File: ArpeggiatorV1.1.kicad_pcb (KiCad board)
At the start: 2 copper layers, 100 x 100 mm, 67 parts, among them J1 DIN-5 MIDI_IN, J2 DIN-5 SYNC_IN, J3 DIN-5 MIDI_OUT, J4 Conn_01x03_Pin, SW1 SW_SYNC, SW2 SW_MODE, SW3 SW_OCT, SW4 SW_ONOFF, SW5 SW_HOLD, U1 6N138, U2 6N138, U3 Pico

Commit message: Minor PCB corrections and cleanups.
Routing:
- net GND: track 32.5 -> 0.00 mm
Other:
- board text added: "MIDI Sync"
- board text removed: "Tempo"
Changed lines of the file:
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@@
     (effects (font (size 2 2) (thickness 0.15)) (justify bottom mirror))
   )
-  (gr_text "Tempo" (at 43.18 123.952) (layer "F.SilkS")
+  (gr_text "MIDI Sync" (at 43.18 123.952) (layer "F.SilkS")
     (effects (font (size 1 1) (thickness 0.15)) (justify bottom))
   )
@@
   (segment (start 55.225 53.975) (end 57.785 56.535) (width 0.4) (layer "F.Cu") (net 1))
   (segment (start 46.99 50.165) (end 50.8 53.975) (width 0.4) (layer "F.Cu") (net 1))
-  (segment (start 132.79 130.52) (end 126.29 130.52) (width 0.6) (layer "F.Cu") (net 2))
-  (segment (start 39.93 130.52) (end 46.43 130.52) (width 0.6) (layer "F.Cu") (net 2))
-  (segment (start 61.52 130.52) (end 68.02 130.52) (width 0.6) (layer "F.Cu") (net 2))
-  (segment (start 79.3 130.52) (end 85.8 130.52) (width 0.6) (layer "F.Cu") (net 2))
-  (segment (start 112.47 130.52) (end 105.97 130.52) (width 0.6) (layer "F.Cu") (net 2))
   (segment (start 61.595 54.61) (end 57.15 50.165) (width 0.4) (layer "F.Cu") (net 3))
   (segment (start 63.67526 43.815) (end 67.31 47.44974) (width 0.4) (layer "F.Cu") (net 3))
@@
   (segment (start 118.095 51.775892) (end 118.293109 51.974001) (width 0.25) (layer "B.Cu") (net 37))
   (segment (start 118.095 45.015) (end 118.095 51.775892) (width 0.25) (layer "B.Cu") (net 37))
-  (segment (start 128.27 83.82) (end 128.27 77.47) (width 0.25) (layer "F.Cu") (net 38))
-  (segment (start 128.27 77.47) (end 132.08 73.66) (width 0.25) (layer "F.Cu") (net 38))
-  (segment (start 132.08 73.66) (end 132.08 59.69) (width 0.25) (layer "F.Cu") (net 38))
-  (segment (start 133.35 88.9) (end 128.27 83.82) (width 0.25) (layer "F.Cu") (net 38))
+  (segment (start 128.27 83.82) (end 128.27 77.47) (width 0.4) (layer "F.Cu") (net 38))
+  (segment (start 128.27 77.47) (end 132.08 73.66) (width 0.4) (layer "F.Cu") (net 38))
+  (segment (start 132.08 73.66) (end 132.08 59.69) (width 0.4) (layer "F.Cu") (net 38))
+  (segment (start 133.35 88.9) (end 128.27 83.82) (width 0.4) (layer "F.Cu") (net 38))
   (segment (start 81.861138 67.471998) (end 78.74 70.593136) (width 0.4) (layer "F.Cu") (net 39))
   (segment (start 59.055 88.265) (end 57.15 90.17) (width 0.4) (layer "F.Cu") (net 39))

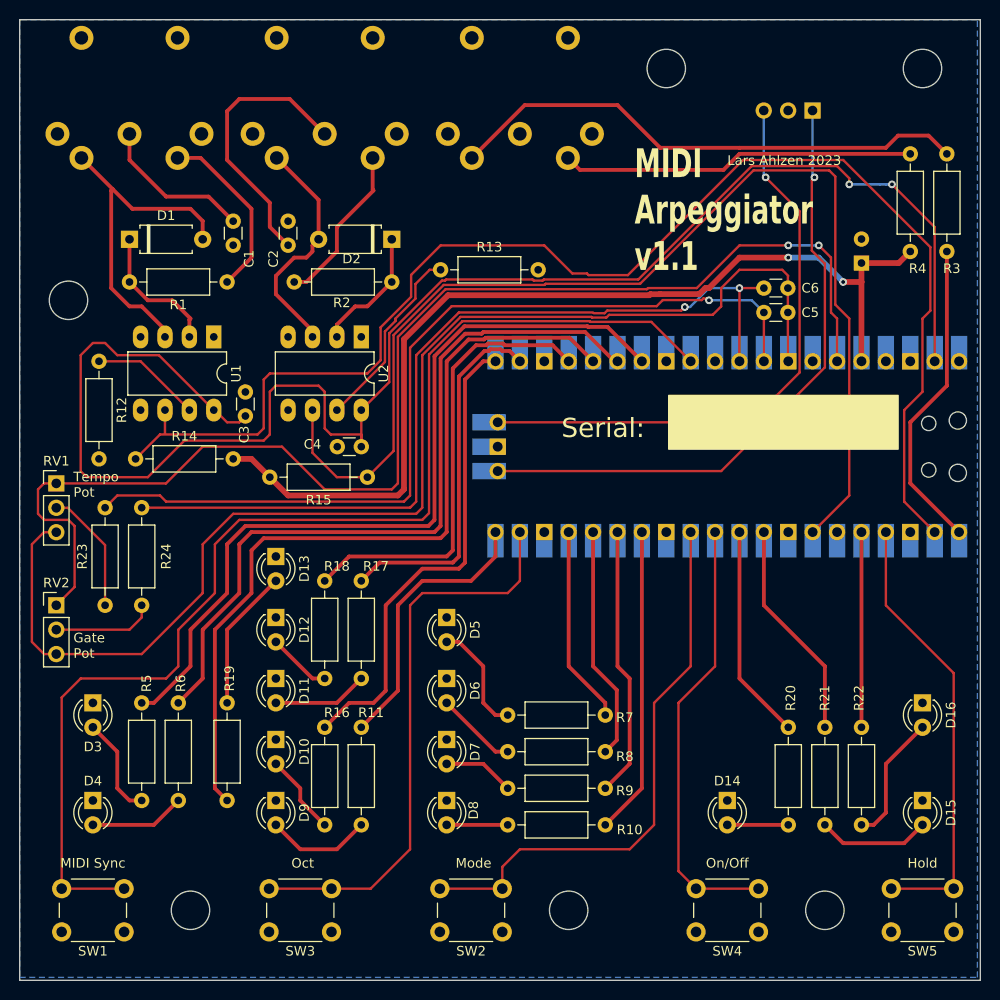
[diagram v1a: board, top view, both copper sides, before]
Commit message: Added component values to PCB silkscreen.
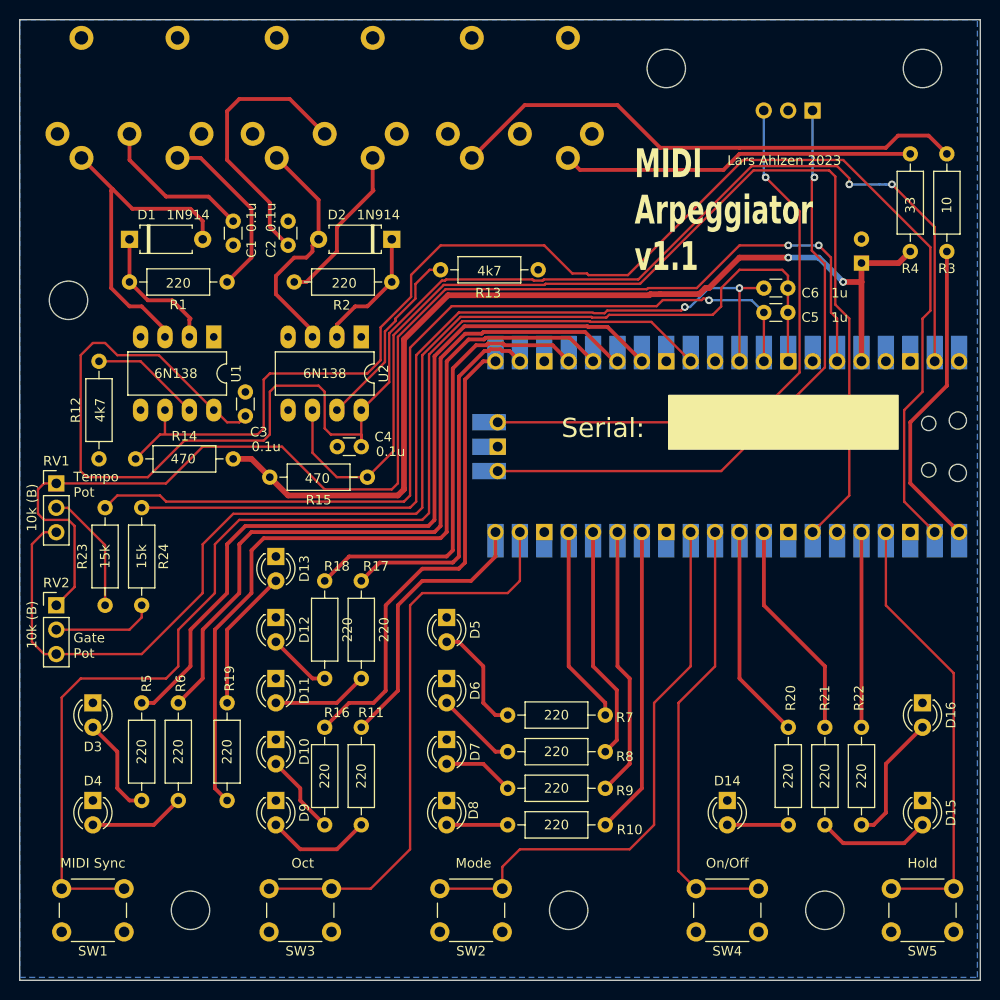
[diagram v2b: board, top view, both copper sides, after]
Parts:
- D10, D11, D12, D13, D15, D16, D3, D4, D5, D6, D7, D8, D9: value LED -> Green
- D14: value LED -> Red
- J1: value DIN-5 MIDI_IN -> DIN-5_MIDI_IN
- J2: value DIN-5 SYNC_IN -> DIN-5_SYNC_IN
- J3: value DIN-5 MIDI_OUT -> DIN-5_MIDI_OUT

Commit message: Updated schematic+PCB with new MIDI interface section.
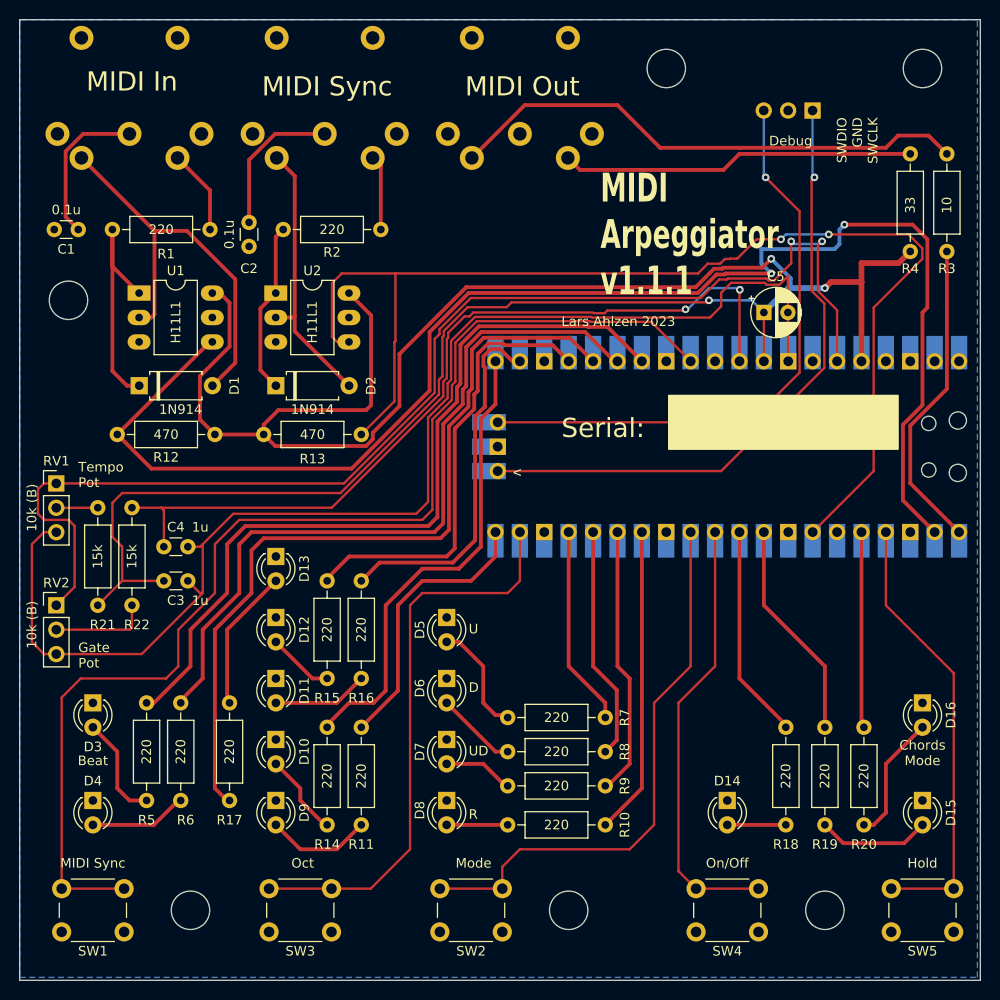
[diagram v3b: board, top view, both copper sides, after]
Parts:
- removed C6: 1u, Capacitor_THT:C_Disc_D3.0mm_W1.6mm_P2.50mm
- removed C7: 10u, Capacitor_THT:CP_Radial_D5.0mm_P2.50mm
- removed R23, R24: 15k, Resistor_THT:R_Axial_DIN0207_L6.3mm_D2.5mm_P10.16mm_Horizontal
- C3, C4: value 0.1u -> 1u
- C5: value 1u -> 10u; footprint Capacitor_THT:C_Disc_D3.0mm_W1.6mm_P2.50mm -> Capacitor_THT:CP_Radial_D5.0mm_P2.50mm
- J1: value DIN-5_MIDI_IN -> DIN-5_FEMALE
- J2: value DIN-5_SYNC_IN -> DIN-5_FEMALE
- J3: value DIN-5_MIDI_OUT -> DIN-5_FEMALE
- R12, R13: value 4k7 -> 470
- R14, R15: value 470 -> 220
- R21, R22: value 220 -> 15k
- SW1: value SW_SYNC -> SW_PUSH
- SW2: value SW_MODE -> SW_PUSH
- SW3: value SW_OCT -> SW_PUSH
- SW4: value SW_ONOFF -> SW_PUSH
- SW5: value SW_HOLD -> SW_PUSH
- U1, U2: value 6N138 -> H11L1; footprint Package_DIP:DIP-8_W7.62mm_LongPads -> Package_DIP:DIP-6_W7.62mm_LongPads
- moved R21 82.6 mm to (43.7, 86.4), turned to -90 degrees
- moved R22 79.3 mm to (47.2, 96.5)
- moved R19 63.5 mm to (119.4, 119.4), turned to 90 degrees
- moved R18 50.4 mm to (115.3, 119.4)
- moved R14 43.0 mm to (67.6, 119.4), turned to 90 degrees
- moved R13 25.2 mm to (61.0, 78.7)
- moved C4 23.0 mm to (50.6, 90.4), turned to 0 degrees
- moved R15 21.0 mm to (71.1, 104.1), turned to 90 degrees
- moved D2 19.4 mm to (62.2, 73.7), turned to 0 degrees
- moved C3 19.1 mm to (50.6, 94.0), turned to 0 degrees
- moved C1 16.2 mm to (41.7, 57.4), turned to 180 degrees
- moved D1 15.3 mm to (48.0, 73.7)
- moved R16 15.2 mm to (67.6, 104.1)
- moved R12 14.3 mm to (55.9, 78.7), turned to 180 degrees
- moved R17 13.9 mm to (57.4, 106.7), turned to -90 degrees
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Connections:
- C3 pad 1: +5V -> /TEMPO
- C3 pad 2: GND -> GNDA
- C4 pad 1: +5V -> /GATE
- C4 pad 2: GND -> GNDA
- C5 pad 1: /TEMPO -> VCC
- C5 pad 2: GNDA -> GND
- R12 pad 1: Net-(U1-VO1) -> VCC
- R12 pad 2: GND -> /MIDI_IN
- R13 pad 1: Net-(U2-VO1) -> VCC
- R13 pad 2: GND -> /MIDI_SYNC_IN
- R14 pad 1: /MIDI_IN -> Net-(D10-A)
- R14 pad 2: VCC -> /OCT2_LED
- R15 pad 1: /MIDI_SYNC_IN -> Net-(D11-A)
- R15 pad 2: VCC -> /OCT3_LED
- R16 pad 1: Net-(D10-A) -> Net-(D12-A)
- R16 pad 2: /OCT2_LED -> /OCT4_LED
- R17 pad 1: Net-(D11-A) -> Net-(D13-A)
- R17 pad 2: /OCT3_LED -> /OCT5_LED
- R18 pad 1: Net-(D12-A) -> Net-(D14-A)
- R18 pad 2: /OCT4_LED -> /ONOFF_LED
- R19 pad 1: Net-(D13-A) -> Net-(D15-A)
- R19 pad 2: /OCT5_LED -> /CHORDS_LED
- R20 pad 1: Net-(D14-A) -> Net-(D16-A)
- R20 pad 2: /ONOFF_LED -> /HOLD_LED
- R21 pad 1: Net-(D15-A) -> Net-(R21-Pad1)
- R21 pad 2: /CHORDS_LED -> /TEMPO
- R22 pad 1: Net-(D16-A) -> Net-(R22-Pad1)
- R22 pad 2: /HOLD_LED -> /GATE
- RV1 pad 2: Net-(R23-Pad1) -> Net-(R21-Pad1)
- RV2 pad 2: Net-(R24-Pad1) -> Net-(R22-Pad1)
- U1 pad 1: unconnected-(U1-NC-Pad1) -> Net-(D1-K)
- U1 pad 2: Net-(D1-K) -> Net-(D1-A)
- U1 pad 3: Net-(D1-A) -> unconnected-(U1-Pad3)
- U1 pad 4: unconnected-(U1-NC-Pad4) -> /MIDI_IN
- U1 pad 6: /MIDI_IN -> VCC
- U2 pad 1: unconnected-(U2-NC-Pad1) -> Net-(D2-K)
- U2 pad 2: Net-(D2-K) -> Net-(D2-A)
- U2 pad 3: Net-(D2-A) -> unconnected-(U2-Pad3)
- U2 pad 4: unconnected-(U2-NC-Pad4) -> /MIDI_SYNC_IN
- U2 pad 6: /MIDI_SYNC_IN -> VCC
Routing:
- net +5V: track 168.5 -> 0.00 mm, vias 2 -> 0
- net VCC: track 103.3 -> 144.1 mm
- net Net-(U2-VO1): track 19.7 -> 0.00 mm
- net Net-(C2-Pad1): track 28.8 -> 15.5 mm
- net Net-(R23-Pad1): track 13.0 -> 0.00 mm
- net Net-(D1-K): track 14.3 -> 25.9 mm
- net Net-(U1-VO1): track 11.5 -> 0.00 mm
- net Net-(R24-Pad1): track 10.7 -> 0.00 mm
- net Net-(R22-Pad1): track 0.00 -> 10.3 mm
- net Net-(J1-Pad4): track 18.6 -> 8.86 mm
- net /TEMPO: track 92.8 -> 102.2 mm
- net Net-(J2-Pad4): track 17.1 -> 7.81 mm
- net /MIDI_IN: track 142.8 -> 151.1 mm, vias 0 -> 2
- net Net-(D1-A): track 35.8 -> 43.7 mm
- net /ADC_VREF: track 133.2 -> 127.0 mm
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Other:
- board text added: "Beat"
- board text added: "Chords Mode"
- board text added: "D"
- board text added: "Debug"
- board text added: "MIDI Arpeggiator v1.1.1"
- board text added: "MIDI In"
- board text added: "MIDI Out"
- board text added: "R"
- board text added: "SWDIO GND SWCLK"
- board text added: "U"
- board text added: "UD"
- board text added: "v"
- board text removed: "MIDI Arpeggiator v1.1"

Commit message: Fixed PCB routing error for TEMPO net. Cleaned up some PCB labels on silkscreen.
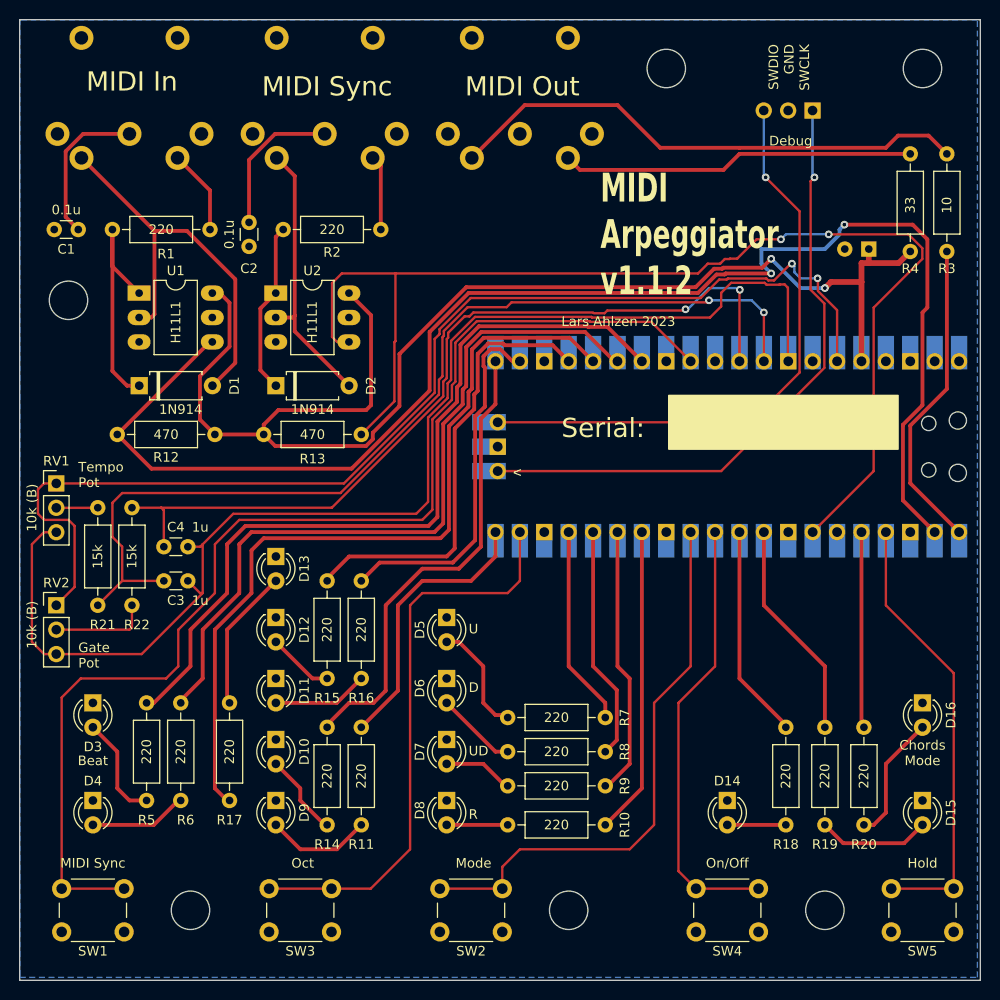
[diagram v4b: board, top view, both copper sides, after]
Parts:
- C5: moved to B.Cu
- moved C5 12.8 mm to (124.0, 59.4), turned to 180 degrees
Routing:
- net /ADC_VREF: track 127.0 -> 121.0 mm
- net VCC: track 144.1 -> 141.7 mm
- net GNDA: track 133.8 -> 132.4 mm
- net /MIDI_IN: track 151.1 -> 150.5 mm
- net /TEMPO: vias 1 -> 2
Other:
- board text added: "J2"
- board text added: "MIDI Arpeggiator v1.1.2"
- board text removed: "MIDI Arpeggiator v1.1.1"
